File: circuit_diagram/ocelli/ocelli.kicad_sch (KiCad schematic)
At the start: 69 parts

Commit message: edit
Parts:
- added BT?: Battery_Cell, symbol Device:Battery_Cell
- added C? (x3): 2.2u, symbol Device:C
- added C? (x2): 1u, symbol Device:C
- added C? (x7): 0.1u, symbol Device:C
- added C?: 4.7u, symbol Device:C
- added C?: 0.01u, symbol Device:C
- added D?: LED, symbol Device:LED
- added FB?: FerriteBead, symbol Device:FerriteBead
- added LS?: PKMCS0909E4000-R1, symbol Device:Speaker_Crystal
- added Q?: TJ8S06M3L, symbol Device:Q_PMOS_GDS
- added Q?: BSS138, symbol Device:Q_NMOS_GSD
- added R? (x3): 1k, symbol Device:R
- added R? (x5): 10k, symbol Device:R
- added R?: 47k, symbol Device:R
- added R?: 100, symbol Device:R
- added R?: 2k, symbol Device:R
- added R?: 100k, symbol Device:R
- added RV?: 10k, symbol Device:R_Potentiometer
- added SW? (x3): TS-06104, symbol Switch:SW_MEC_5E
- added SW? (x2): SW_Push, symbol Switch:SW_Push
- added SW?: SW_SPDT, symbol Switch:SW_SPDT
- added U?: STM32F405RGTx, Package_QFP:LQFP-64_10x10mm_P0.5mm, symbol MCU_ST_STM32F4:STM32F405RGTx
- added U?: NJM2845DL1-33, symbol ocelli_lib:NJM2845DL1-33
- added Y?: Crystal_GND2, symbol Device:Crystal_GND2
- added Y?: Crystal_GND24, symbol Device:Crystal_GND24
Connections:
- net +3.3V: now also C?.1, C?.1, C?.2, C?.2, C?.2, C?.2, FB?.1, LS?.1, R?.1, R?.1, R?.1, R?.1, R?.1, RV?.1, SW?.1, U?.1 (VBAT), U?.19 (VDD), U?.3 (Vout), U?.32 (VDD), U?.48 (VDD), U?.64 (VDD); no longer Q?.1 (C), Q?.1 (C), Q?.1 (C), Q?.1 (C)
- net 3.3_L: no longer C?.1, J?.1 (Pin_1), R?.1, U?.11 (VDDp)
- net 3.3_R: no longer C?.1, J?.1 (Pin_1), R?.1, U?.11 (VDDp)
- net GND: now also BT?.2 (-), C?.1, C?.1, C?.1, C?.1, C?.2, C?.2, C?.2, C?.2, C?.2, C?.2, C?.2, C?.2, C?.2, C?.2, D?.1 (K), Q?.2 (S), R?.2, R?.2, R?.2, R?.2, SW?.1 (A), SW?.2, SW?.3 (K), SW?.3 (K), SW?.3 (K), SW?.4 (A), SW?.4 (A), SW?.4 (A), U?.12 (VSSA), U?.18 (VSS), U?.2 (GND), U?.63 (VSS)
- net +7.5V renamed +BATT
- net +BATT: now also C?.1, Q?.2 (D), R?.1, U?.1 (Vin)
- new net: D?.2 (A), R?.2
- new net: R?.1, U?.28 (PB2)
- new net: Q?.1 (G), R?.2, SW?.2 (B)
- new net: BT?.1 (+), Q?.3 (S), R?.1
- new net: Q?.1 (G), R?.1, R?.1
- new net: LS?.2, Q?.3 (D), R?.2
- new net: C?.1, U?.47 (VCAP_2)
- new net: C?.1, U?.31 (VCAP_1)
- new net: R?.2, RV?.2
- new net +3.3VA: C?.1, C?.1, C?.1, FB?.2, Q?.1 (C), Q?.1 (C), Q?.1 (C), Q?.1 (C), U?.13 (VDDA)
- new net 3.3V_L: C?.1, J?.1 (Pin_1), R?.1, U?.11 (VDDp)
- new net 3.3V_R: C?.1, J?.1 (Pin_1), R?.1, U?.11 (VDDp)
- new net BOOT: R?.1, SW?.2, U?.60 (BOOT0)
- new net BUZZER: RV?.3
- new net NRST: C?.1, SW?.1, U?.7 (NRST)
- new net SW_1: R?.2, SW?.1, SW?.2
- new net SW_2: R?.2, SW?.1, SW?.2
- new net SW_3: R?.2, SW?.1, SW?.2
- new net VBAT_AD: C?.1, R?.1, R?.2
- no-connect marks 8 -> 9
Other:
- removed sheet micon
- moved on the sheet: C?, D?, J?, Q?, R?, U?

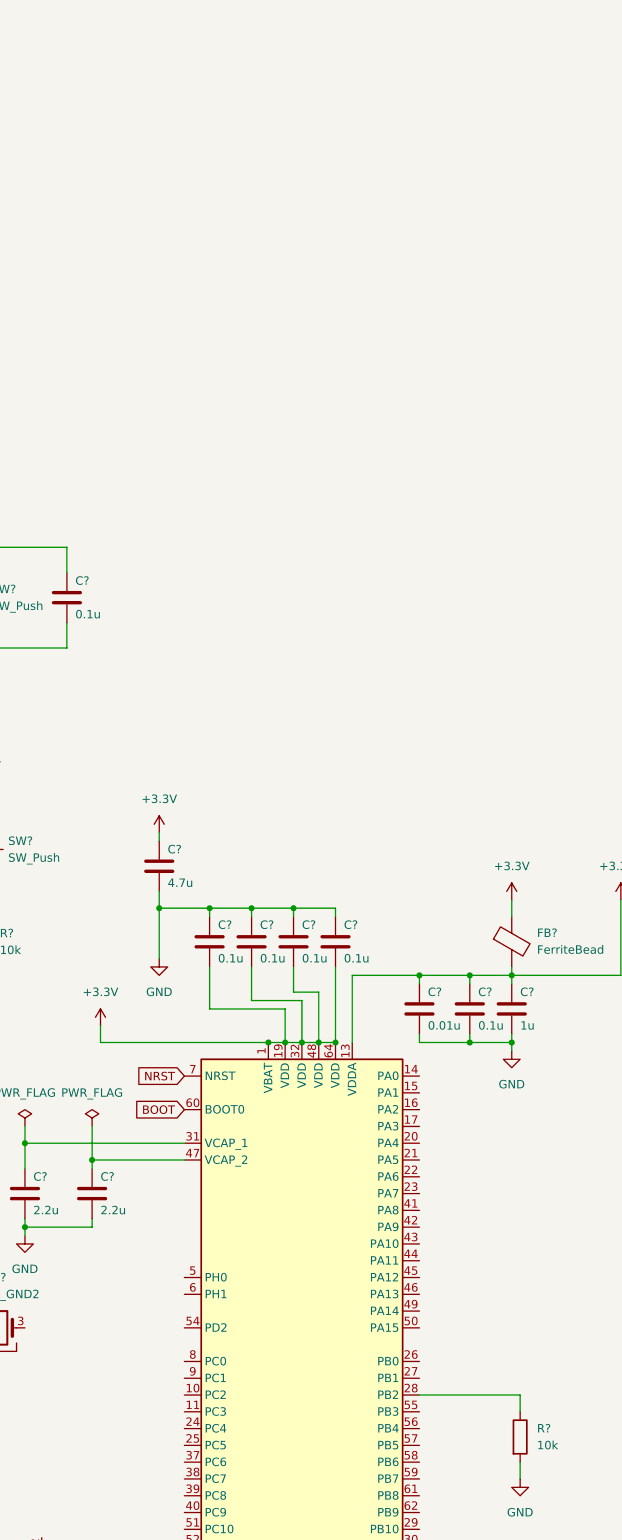
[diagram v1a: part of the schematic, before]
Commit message: 書き込みコネクタ追加
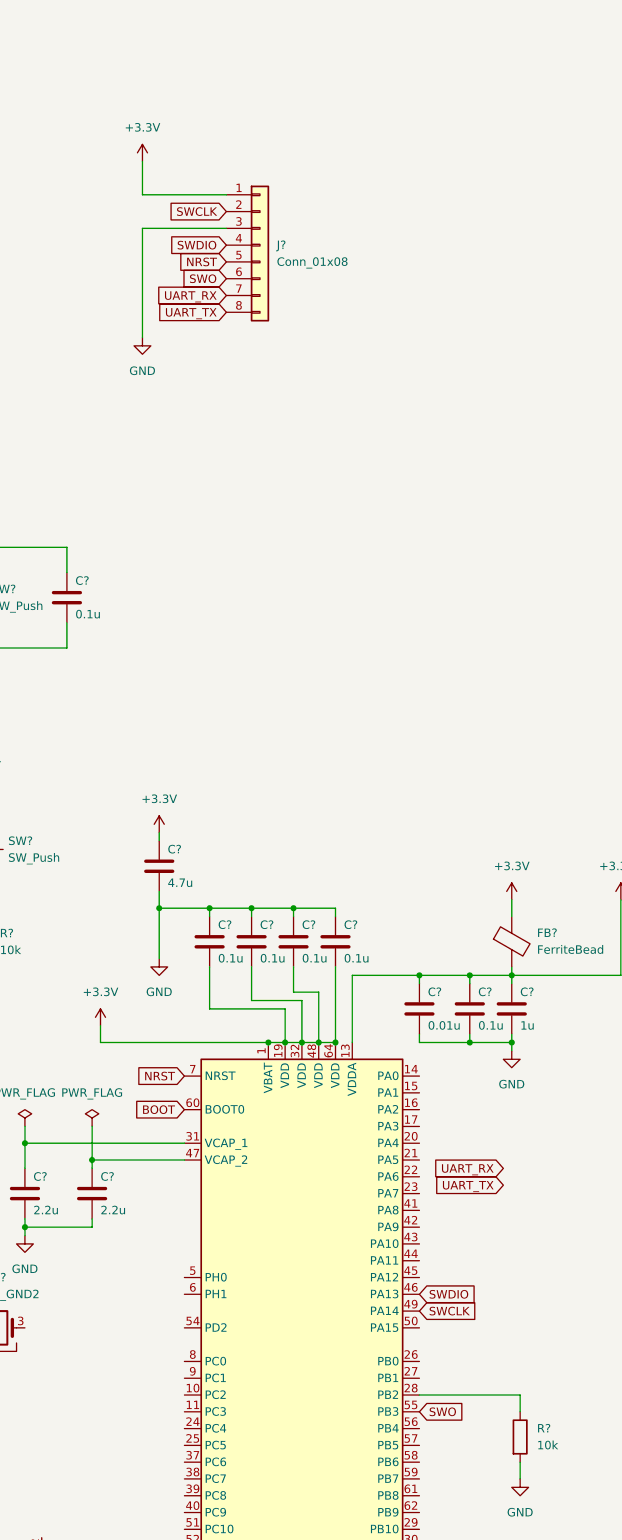
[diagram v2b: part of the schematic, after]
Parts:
- added J?: Conn_01x08, symbol Connector_Generic:Conn_01x08
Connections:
- net +3.3V: now also J?.1 (Pin_1)
- net GND: now also J?.3 (Pin_3)
- net NRST: now also J?.5 (Pin_5)
- net SWDIO: now reaches U?.46 (PA13)
- net SWDIO: now also J?.4 (Pin_4)
- net SWCLK: now reaches U?.49 (PA14)
- net SWCLK: now also J?.2 (Pin_2)
- net SWO: now reaches U?.55 (PB3)
- net SWO: now also J?.6 (Pin_6)
- new net UART_RX: J?.7 (Pin_7)
- new net UART_TX: J?.8 (Pin_8)
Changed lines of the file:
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@@
     (stroke (width 0) (type default) (color 0 0 0 0))
   )
+  (wire (pts (xy 222.25 43.18) (xy 222.25 48.26))
+    (stroke (width 0) (type default) (color 0 0 0 0))
+  )
   (wire (pts (xy 195.58 101.6) (xy 210.82 101.6))
     (stroke (width 0) (type default) (color 0 0 0 0))
@@
     (stroke (width 0) (type default) (color 0 0 0 0))
   )
+  (wire (pts (xy 234.95 53.34) (xy 222.25 53.34))
+    (stroke (width 0) (type default) (color 0 0 0 0))
+  )
   (polyline (pts (xy 120.65 191.77) (xy 120.65 271.78))
     (stroke (width 0) (type default) (color 0 0 0 0))
@@
     (stroke (width 0) (type default) (color 0 0 0 0))
   )
+  (wire (pts (xy 222.25 48.26) (xy 234.95 48.26))
+    (stroke (width 0) (type default) (color 0 0 0 0))
+  )
   (wire (pts (xy 360.68 118.11) (xy 360.68 119.38))
     (stroke (width 0) (type default) (color 0 0 0 0))
@@
     (stroke (width 0) (type default) (color 0 0 0 0))
   )
+  (wire (pts (xy 222.25 53.34) (xy 222.25 69.85))
+    (stroke (width 0) (type default) (color 0 0 0 0))
+  )
   (wire (pts (xy 360.68 46.99) (xy 360.68 49.53))
     (stroke (width 0) (type default) (color 0 0 0 0))
@@
     )
   )
+  (global_label "SWCLK" (shape input) (at 264.16 217.17 0) (fields_autoplaced)
+    (effects (font (size 1.27 1.27)) (justify left))
+    (property "Intersheet References" "${INTERSHEET_REFS}" (id 0) (at 272.8021 217.2494 0)
+      (effects (font (size 1.27 1.27)) (justify left) hide)
+    )
+  )
   (global_label "ENC_CS_R" (shape input) (at 81.28 262.89 180) (fields_autoplaced)
     (effects (font (size 1.27 1.27)) (justify right))
@@
     )
   )
+  (global_label "SWDIO" (shape input) (at 264.16 214.63 0) (fields_autoplaced)
+    (effects (font (size 1.27 1.27)) (justify left))
+    (property "Intersheet References" "${INTERSHEET_REFS}" (id 0) (at 272.4393 214.7094 0)
+      (effects (font (size 1.27 1.27)) (justify left) hide)
+    )
+  )
   (global_label "RIGHT_MOTOR+" (shape input) (at 328.93 30.48 180) (fields_autoplaced)
     (effects (font (size 1.27 1.27)) (justify right))
@@
     )
   )
+  (global_label "SWDIO" (shape input) (at 234.95 55.88 180) (fields_autoplaced)
+    (effects (font (size 1.27 1.27)) (justify right))
+    (property "Intersheet References" "${INTERSHEET_REFS}" (id 0) (at 226.6707 55.8006 0)
+      (effects (font (size 1.27 1.27)) (justify right) hide)
+    )
+  )
   (global_label "DIR_L" (shape input) (at 369.57 81.28 0) (fields_autoplaced)
     (effects (font (size 1.27 1.27)) (justify left))
@@
     )
   )
+  (global_label "UART_RX" (shape input) (at 234.95 63.5 180) (fields_autoplaced)
+    (effects (font (size 1.27 1.27)) (justify right))
+    (property "Intersheet References" "${INTERSHEET_REFS}" (id 0) (at 224.4331 63.4206 0)
+      (effects (font (size 1.27 1.27)) (justify right) hide)
+    )
+  )
   (global_label "ENC_MOSI_R" (shape input) (at 81.28 255.27 180) (fields_autoplaced)
     (effects (font (size 1.27 1.27)) (justify right))
@@
     )
   )
+  (global_label "SWO" (shape input) (at 264.16 232.41 0) (fields_autoplaced)
+    (effects (font (size 1.27 1.27)) (justify left))
+    (property "Intersheet References" "${INTERSHEET_REFS}" (id 0) (at 270.5645 232.4894 0)
+      (effects (font (size 1.27 1.27)) (justify left) hide)
+    )
+  )
   (global_label "GND_L" (shape input) (at 104.14 193.04 0) (fields_autoplaced)
     (effects (font (size 1.27 1.27)) (justify left))
@@
     )
   )
+  (global_label "UART_TX" (shape input) (at 234.95 66.04 180) (fields_autoplaced)
+    (effects (font (size 1.27 1.27)) (justify right))
+    (property "Intersheet References" "${INTERSHEET_REFS}" (id 0) (at 224.7355 65.9606 0)
+      (effects (font (size 1.27 1.27)) (justify right) hide)
+    )
+  )
   (global_label "SCLK" (shape input) (at 25.4 208.28 180) (fields_autoplaced)
     (effects (font (size 1.27 1.27)) (justify right))
@@
     )
   )
+  (global_label "NRST" (shape input) (at 234.95 58.42 180) (fields_autoplaced)
+    (effects (font (size 1.27 1.27)) (justify right))
+    (property "Intersheet References" "${INTERSHEET_REFS}" (id 0) (at 227.7593 58.3406 0)
+      (effects (font (size 1.27 1.27)) (justify right) hide)
+    )
+  )
   (global_label "MOSI" (shape input) (at 140.97 215.9 90) (fields_autoplaced)
     (effects (font (size 1.27 1.27)) (justify left))
@@
     )
   )
+  (global_label "UART_TX" (shape input) (at 276.86 198.12 180) (fields_autoplaced)
+    (effects (font (size 1.27 1.27)) (justify right))
+    (property "Intersheet References" "${INTERSHEET_REFS}" (id 0) (at 266.6455 198.0406 0)
+      (effects (font (size 1.27 1.27)) (justify right) hide)
+    )
+  )
   (global_label "ENC_MOSI_R" (shape input) (at 54.61 255.27 180) (fields_autoplaced)
     (effects (font (size 1.27 1.27)) (justify right))
@@
     )
   )
+  (global_label "UART_RX" (shape input) (at 276.86 195.58 180) (fields_autoplaced)
+    (effects (font (size 1.27 1.27)) (justify right))
+    (property "Intersheet References" "${INTERSHEET_REFS}" (id 0) (at 266.3431 195.5006 0)
+      (effects (font (size 1.27 1.27)) (justify right) hide)
+    )
+  )
   (global_label "ENC_CS_L" (shape input) (at 81.28 210.82 180) (fields_autoplaced)
     (effects (font (size 1.27 1.27)) (justify right))
@@
     )
   )
+  (global_label "SWCLK" (shape input) (at 234.95 50.8 180) (fields_autoplaced)
+    (effects (font (size 1.27 1.27)) (justify right))
+    (property "Intersheet References" "${INTERSHEET_REFS}" (id 0) (at 226.3079 50.7206 0)
+      (effects (font (size 1.27 1.27)) (justify right) hide)
+    )
+  )
   (global_label "LED3" (shape input) (at 391.16 27.94 90) (fields_autoplaced)
     (effects (font (size 1.27 1.27)) (justify left))
@@
     )
   )
+  (global_label "SWO" (shape input) (at 234.95 60.96 180) (fields_autoplaced)
+    (effects (font (size 1.27 1.27)) (justify right))
+    (property "Intersheet References" "${INTERSHEET_REFS}" (id 0) (at 228.5455 60.8806 0)
+      (effects (font (size 1.27 1.27)) (justify right) hide)
+    )
+  )
   (symbol (lib_id "power:+3.3V") (at 170.18 237.49 0) (unit 1)
     (in_bom yes) (on_board yes) (fields_autoplaced)
@@
     (pin "1")
   )
+  (symbol (lib_id "power:+3.3V") (at 222.25 43.18 0) (unit 1)
+    (in_bom yes) (on_board yes) (fields_autoplaced)
+    (property "Reference" "#PWR?" (id 0) (at 222.25 46.99 0)
+      (effects (font (size 1.27 1.27)) hide)
+    )
+    (property "Value" "+3.3V" (id 1) (at 222.25 38.1 0))
+    (property "Footprint" "" (id 2) (at 222.25 43.18 0)
+      (effects (font (size 1.27 1.27)) hide)
+    )
+    (property "Datasheet" "" (id 3) (at 222.25 43.18 0)
+      (effects (font (size 1.27 1.27)) hide)
+    )
+    (pin "1")
+  )
   (symbol (lib_id "Device:R") (at 107.95 157.48 0) (unit 1)
     (in_bom yes) (on_board yes) (fields_autoplaced)
@@
     (pin "2")
   )
+  (symbol (lib_id "power:GND") (at 222.25 69.85 0) (unit 1)
+    (in_bom yes) (on_board yes) (fields_autoplaced)
+    (property "Reference" "#PWR?" (id 0) (at 222.25 76.2 0)
+      (effects (font (size 1.27 1.27)) hide)
+    )
+    (property "Value" "GND" (id 1) (at 222.25 74.93 0))
+    (property "Footprint" "" (id 2) (at 222.25 69.85 0)
+      (effects (font (size 1.27 1.27)) hide)
+    )
+    (property "Datasheet" "" (id 3) (at 222.25 69.85 0)
+      (effects (font (size 1.27 1.27)) hide)
+    )
+    (pin "1")
+  )
   (symbol (lib_id "Device:R") (at 370.84 31.75 0) (unit 1)
     (in_bom yes) (on_board yes) (fields_autoplaced)
@@
     (pin "1")
   )
+  (symbol (lib_id "Connector_Generic:Conn_01x08") (at 240.03 55.88 0) (unit 1)
+    (in_bom yes) (on_board yes) (fields_autoplaced)
+    (property "Reference" "J?" (id 0) (at 242.57 55.8799 0)
+      (effects (font (size 1.27 1.27)) (justify left))
+    )
+    (property "Value" "Conn_01x08" (id 1) (at 242.57 58.4199 0)
+      (effects (font (size 1.27 1.27)) (justify left))
+    )
+    (property "Footprint" "" (id 2) (at 240.03 55.88 0)
+      (effects (font (size 1.27 1.27)) hide)
+    )
+    (property "Datasheet" "~" (id 3) (at 240.03 55.88 0)
+      (effects (font (size 1.27 1.27)) hide)
+    )
+    (pin "1")
+    (pin "2")
+    (pin "3")
+    (pin "4")
+    (pin "5")
+    (pin "6")
+    (pin "7")
+    (pin "8")
+  )
   (symbol (lib_id "power:+3.3V") (at 21.59 200.66 0) (unit 1)
     (in_bom yes) (on_board yes) (fields_autoplaced)
@@
       (reference "#PWR?") (unit 1) (value "GND") (footprint "")
     )
+    (path "/36169bbb-0264-48ca-aa31-e1196cd15920"
+      (reference "#PWR?") (unit 1) (value "+3.3V") (footprint "")
+    )
     (path "/3df9cdb4-9f32-465c-988f-45ed2a462fa3"
       (reference "#PWR?") (unit 1) (value "GND") (footprint "")
@@
       (reference "#PWR?") (unit 1) (value "+3.3VA") (footprint "")
     )
+    (path "/a55d701f-013a-4a22-9fe4-f06cee49b313"
+      (reference "#PWR?") (unit 1) (value "GND") (footprint "")
+    )
     (path "/b5282f18-23b9-4b62-96dc-181f43eaa436"
       (reference "#PWR?") (unit 1) (value "GND") (footprint "")
@@
       (reference "J?") (unit 1) (value "Conn_01x02") (footprint "")
     )
+    (path "/d090d542-ee13-400b-8740-d2e8671874d8"
+      (reference "J?") (unit 1) (value "Conn_01x08") (footprint "")
+    )
     (path "/ebbfddba-9979-4b3e-be74-89ea6ffec038"

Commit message: 回路図PDF追加
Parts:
- removed Y?: Crystal_GND2, symbol Device:Crystal_GND2
- removed Y?: Crystal_GND24, symbol Device:Crystal_GND24
- added R28, R5, R6: 10k, symbol Device:R
- FB1: renamed from FB?; value FerriteBead -> MZ1608-102Y
- gave numbers to parts that had none: 110
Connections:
- net 3.3_L is gone; now on net 3.3V_L: U2.14 (WM)
- net 3.3_R is gone; now on net 3.3V_R: U3.14 (WM)
- net CS_IMU is gone; now on net SPI1_CS: U4.22 (nCS)
- net CS_L is gone; now on net SPI2_CS0: J1.5 (Pin_5)
- net CS_R is gone; now on net SPI2_CS1: J2.5 (Pin_5)
- net LEFT_FRONT is gone; now on net LEFT_FRONT_IR: R25.1
- net LEFT_SIDE is gone; now on net LEFT_SIDE_IR: R11.2
- net RIGHT_FRONT is gone; now on net RIGHT_FRONT_IR: R16.1
- net RIGHT_SIDE is gone; now on net RIGHT_SIDE_IR: R1.2
- net SW_3 is gone; now on net SW_2: R32.2, SW4.1, SW4.2
- net +3.3V: now also C30.2, R28.1, R5.1, R6.1; no longer C30.1
- net BUZZER: now also U5.57 (PB5)
- net DIR_L: now also U5.43 (PA10)
- net DIR_R: now also U5.44 (PA11)
- net GND: now also C30.1; no longer C30.2
- net LED0: now also U5.40 (PC9)
- net LED1: now also U5.39 (PC8)
- net LED2: now also U5.38 (PC7)
- net LED3: now also U5.37 (PC6)
- net LEFT_FRONT_AD: now also U5.26 (PB0)
- net LEFT_SIDE_AD: now also U5.27 (PB1)
- net PWM_L: now also U5.41 (PA8)
- net PWM_R: now also U5.42 (PA9)
- net RIGHT_FRONT_AD: now also U5.25 (PC5)
- net RIGHT_SIDE_AD: now also U5.24 (PC4)
- net SW_1: now also R31.2, SW3.1, SW3.2, U5.35 (PB14); no longer R24.2, SW2.1, SW2.2
- net SW_2: now also U5.34 (PB13); no longer R31.2, SW3.1, SW3.2
- net UART_RX: now also U5.17 (PA3)
- net UART_TX: now also U5.16 (PA2)
- net VBAT_AD: now also U5.8 (PC0)
- net SPI2_MISO: now reaches U5.10 (PC2)
- net SPI2_MISO: now also J1.3 (Pin_3), J2.3 (Pin_3)
- net SPI2_MOSI: now reaches U5.11 (PC3)
- net SPI2_MOSI: now also J1.2 (Pin_2), J2.2 (Pin_2)
- net RIGHT_SIDE_IR: now reaches U5.14 (PA0)
- net RIGHT_FRONT_IR: now reaches U5.15 (PA1)
- net SPI2_CS1: now reaches U5.2 (PC13)
- net SPI2_CS1: now also R6.2
- net SPI1_CS: now reaches U5.20 (PA4)
- net SPI1_CS: now also R28.2
- net SPI1_SCLK: now reaches U5.21 (PA5)
- net SPI1_SCLK: now also U4.23 (SCL/SCLK)
- net SPI1_MISO: now reaches U5.22 (PA6)
- net SPI1_MISO: now also U4.9 (SDO/AD0)
- net SPI1_MOSI: now reaches U5.23 (PA7)
- net SPI1_MOSI: now also U4.24 (SDA/SDI)
- net SPI2_SCLK: now reaches U5.29 (PB10)
- net SPI2_SCLK: now also J1.4 (Pin_4), J2.4 (Pin_4)
- net LEFT_FRONT_IR: now reaches U5.30 (PB11)
- net LEFT_SIDE_IR: now reaches U5.33 (PB12)
- net SW_0: now reaches U5.36 (PB15)
- net SW_0: now also R24.2, SW2.1, SW2.2
- net SPI2_CS0: now reaches U5.9 (PC1)
- net SPI2_CS0: now also R5.2
- removed net MISO: J1.3 (Pin_3), J2.3 (Pin_3), U4.9 (SDO/AD0)
- removed net MOSI: J1.2 (Pin_2), J2.2 (Pin_2), U4.24 (SDA/SDI)
- removed net SCLK: J1.4 (Pin_4), J2.4 (Pin_4), U4.23 (SCL/SCLK)
- no-connect marks 9 -> 24
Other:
- note added: "Buzzer"
- note added: "Encoder"
- note added: "LED"
- note added: "Micon"
- note added: "Power"
- note added: "Switch"
- moved on the sheet: BT1, C1, C10, C11, C12, C13, C14, C15, C16, C17, C18, C19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

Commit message: スタイル調整
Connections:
- net +3.3V: now also C30.1; no longer C30.2
- net +BATT: now also C28.1, C29.1; no longer C28.2, C29.2
- net GND: now also C28.2, C29.2, C30.2; no longer C28.1, C29.1, C30.1
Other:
- moved on the sheet: C28, C29, C30, R40, U6
